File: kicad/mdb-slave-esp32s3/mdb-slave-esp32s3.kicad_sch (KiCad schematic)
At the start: 36 parts, among them J1 Conn_02x09_Odd_Even, J2 MDB_Connector, P1 USB_C_Plug_USB2.0, SW1 Reset, SW2 Boot, U1 ESP32-S3, U2 LM317_SOT-223, U4 PC817, U5 PC817, Y1 Crystal

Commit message: Refacting
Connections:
- net mdb_slave_receive renamed io4
- net mdb_slave_transmit renamed io5
- net vdd_spi: no longer names the net of U1.29 (VDD_SPI)
- no-connect marks 23 -> 24
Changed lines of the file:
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@@
+	)
+	(no_connect
+		(at 124.46 134.62)
 	)
 	(no_connect
@@
 	(wire
 		(pts
-			(xy 124.46 128.27) (xy 124.46 134.62)
-		)
-		(stroke
-			(width 0)
-			(type default)
-		)
-	)
-	(wire
-		(pts
 			(xy 165.1 170.18) (xy 167.64 170.18)
 		)
@@
 	(wire
 		(pts
-			(xy 165.1 167.64) (xy 186.69 167.64)
-		)
-		(stroke
-			(width 0)
-			(type default)
-		)
-	)
-	(wire
-		(pts
 			(xy 99.06 160.02) (xy 93.98 160.02)
 		)
@@
 	(wire
 		(pts
-			(xy 165.1 165.1) (xy 186.69 165.1)
-		)
-		(stroke
-			(width 0)
-			(type default)
-		)
-	)
-	(wire
-		(pts
 			(xy 165.1 195.58) (xy 167.64 195.58)
 		)
@@
 	(wire
 		(pts
+			(xy 165.1 165.1) (xy 167.64 165.1)
+		)
+		(stroke
+			(width 0)
+			(type default)
+		)
+	)
+	(wire
+		(pts
 			(xy 45.72 240.03) (xy 57.15 240.03)
 		)
@@
 		(pts
 			(xy 53.34 255.27) (xy 57.15 255.27)
+		)
+		(stroke
+			(width 0)
+			(type default)
+		)
+	)
+	(wire
+		(pts
+			(xy 165.1 167.64) (xy 167.64 167.64)
 		)
 		(stroke
@@
 		)
 	)
+	(label "io5"
+		(at 167.64 167.64 0)
+		(fields_autoplaced yes)
+		(effects
+			(font
+				(size 1.27 1.27)
+			)
+			(justify left bottom)
+		)
+	)
 	(label "io2"
 		(at 53.34 250.19 180)
@@
 		)
 	)
+	(label "io5"
+		(at 356.87 110.49 0)
+		(fields_autoplaced yes)
+		(effects
+			(font
+				(size 1.27 1.27)
+			)
+			(justify left bottom)
+		)
+	)
 	(label "io14"
 		(at 167.64 190.5 0)
@@
 		)
 	)
-	(label "mdb_slave_receive"
-		(at 186.69 165.1 0)
-		(fields_autoplaced yes)
-		(effects
-			(font
-				(size 1.27 1.27)
-			)
-			(justify left bottom)
-		)
-	)
 	(label "io10"
 		(at 73.66 245.11 0)
@@
 		)
 	)
+	(label "io4"
+		(at 167.64 165.1 0)
+		(fields_autoplaced yes)
+		(effects
+			(font
+				(size 1.27 1.27)
+			)
+			(justify left bottom)
+		)
+	)
 	(label "io6"
 		(at 167.64 170.18 0)
@@
 		)
 	)
-	(label "mdb_slave_receive"
-		(at 356.87 95.25 0)
-		(fields_autoplaced yes)
-		(effects
-			(font
-				(size 1.27 1.27)
-			)
-			(justify left bottom)
-		)
-	)
 	(label "io7"
 		(at 167.64 172.72 0)
@@
 		)
 	)
+	(label "io4"
+		(at 356.87 95.25 0)
+		(fields_autoplaced yes)
+		(effects
+			(font
+				(size 1.27 1.27)
+			)
+			(justify left bottom)
+		)
+	)
 	(label "io21"
 		(at 177.8 59.69 0)
@@
 		)
 	)
-	(label "vdd_spi"
-		(at 124.46 128.27 90)
-		(fields_autoplaced yes)
-		(effects
-			(font
-				(size 1.27 1.27)
-			)
-			(justify left bottom)
-		)
-	)
 	(label "mdb_master_receive"
 		(at 325.12 115.57 180)
@@
 		)
 	)
-	(label "mdb_slave_transmit"
-		(at 356.87 110.49 0)
-		(fields_autoplaced yes)
-		(effects
-			(font
-				(size 1.27 1.27)
-			)
-			(justify left bottom)
-		)
-	)
 	(label "io9"
 		(at 167.64 177.8 0)
@@
 		(fields_autoplaced yes)
 		(effects
-			(font
-				(size 1.27 1.27)
-			)
-			(justify left bottom)
-		)
-	)
-	(label "mdb_slave_transmit"
-		(at 186.69 167.64 0)
-		(fields_autoplaced yes)
-		(effects

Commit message: refacting
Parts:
- removed AE1: Antenna, RF_Antenna:Texas_SWRA117D_2.4GHz_Right, symbol Device:Antenna
- removed C1, C2, C3, C4, C5, C6: C, Capacitor_SMD:C_0603_1608Metric, symbol Device:C
- removed D1, D2: LED, LED_SMD:LED_0603_1608Metric, symbol Device:LED
- removed D4: D, Diode_SMD:D_SOD-123, symbol Device:D
- removed L1: 47nH, Inductor_SMD:L_0603_1608Metric, symbol Device:L
- removed P1: USB_C_Plug_USB2.0, Connector_USB:USB_C_Receptacle_G-Switch_GT-USB-7010ASV, symbol Connector:USB_C_Plug_USB2.0
- removed R1, R10, R2, R3, R4, R5, R6, R7, R9: R, Resistor_SMD:R_0603_1608Metric, symbol Device:R
- removed SW2: Boot, Button_Switch_SMD:SW_Tactile_SPST_NO_Straight_CK_PTS636Sx25SMTRLFS, symbol Switch:SW_Push
- removed U1: ESP32-S3, Package_DFN_QFN:QFN-56-1EP_7x7mm_P0.4mm_EP5.6x5.6mm, symbol PCM_Espressif:ESP32-S3
- removed Y1: Crystal, Crystal:Crystal_HC49-4H_Vertical, symbol Device:Crystal
- added AE2: Antenna, RF_Antenna:Texas_SWRA117D_2.4GHz_Right, symbol Device:Antenna
- added C10, C11, C12, C13, C14, C15, C8: C, Capacitor_SMD:C_0603_1608Metric, symbol Device:C
- added D3: D, Diode_SMD:D_SOD-123, symbol Device:D
- added D6, D7: LED, LED_SMD:LED_0603_1608Metric, symbol Device:LED
- added L2: 47nH, Inductor_SMD:L_0603_1608Metric, symbol Device:L
- added P2: USB_C_Plug_USB2.0, Connector_USB:USB_C_Receptacle_G-Switch_GT-USB-7010ASV, symbol Connector:USB_C_Plug_USB2.0
- added R15, R16, R17, R18, R19, R20, R22, R23, R24: R, Resistor_SMD:R_0603_1608Metric, symbol Device:R
- added SW3: SW_Push, Button_Switch_SMD:SW_Tactile_SPST_NO_Straight_CK_PTS636Sx25SMTRLFS, symbol Switch:SW_Push
- added TP1, TP2, TP3: TestPoint, TestPoint:TestPoint_Pad_D1.0mm, symbol Connector:TestPoint
- added U3: ESP32-S3, Package_DFN_QFN:QFN-56-1EP_7x7mm_P0.4mm_EP5.6x5.6mm, symbol PCM_Espressif:ESP32-S3
- added U6: W25Q32JVSS, Package_SON:WSON-8-1EP_8x6mm_P1.27mm_EP3.4x4.3mm, symbol Memory_Flash:W25Q32JVSS
- added Y2: Crystal, Crystal:Crystal_HC49-4H_Vertical, symbol Device:Crystal
- SW1: value Reset -> SW_Push
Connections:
- net +3V3: now also J1.16 (Pin_16), C12.2, C13.2, C14.2, D7.2 (A), R15.1, R17.2, TP1.1, U3.2 (VDD3P3), U3.20 (VDD3P3_RTC), U3.3 (VDD3P3), U3.46 (VDD3P3_CPU), U3.55 (VDDA), U3.56 (VDDA)
- net GND: now also SW1.2, C10.1, C11.1, C12.1, C13.1, C14.1, C15.2, L2.2, P2.A1 (GND), P2.A12 (GND), P2.B1 (GND), P2.B12 (GND), R16.2, R18.2, R19.2, R20.2, R22.1, R23.1, R24.2, SW3.1, TP3.1, U3.57 (GND), U6.4 (GND); no longer J1.16 (Pin_16), SW1.1
- net boot: now also SW1.1, R17.1, U3.5 (GPIO0/BOOT)
- net io1: now also U3.6 (GPIO1/ADC1_CH0)
- net io10: now also U3.15 (GPIO10/ADC1_CH9)
- net io11: now also U3.16 (GPIO11/ADC2_CH0)
- net io12: now also U3.17 (GPIO12/ADC2_CH1)
- net io13: now also U3.18 (GPIO13/ADC2_CH2)
- net io14: now also U3.19 (GPIO14/ADC2_CH3)
- net io17: now also U3.23 (GPIO17/ADC2_CH6)
- net io18: now also U3.24 (GPIO18/ADC2_CH7)
- net io2: now also U3.7 (GPIO2/ADC1_CH1)
- net io21: now also D6.2 (A), U3.27 (GPIO21)
- net io4: now also U3.9 (GPIO4/ADC1_CH3)
- net io5: now also U3.10 (GPIO5/ADC1_CH4)
- net io6: now also U3.11 (GPIO6/ADC1_CH5)
- net io7: now also U3.12 (GPIO7/ADC1_CH6)
- net io8: now also U3.13 (GPIO8/ADC1_CH7)
- net io9: now also U3.14 (GPIO9/ADC1_CH8)
- net u0rxd: now also U3.50 (U0RXD/PROG/GPIO44)
- net u0txd: now also U3.49 (U0TXD/PROG/GPIO43)
- net usb+: now also P2.A6 (D+), U3.26 (GPIO20/USB_D+/ADC2_CH9)
- net usb-: now also P2.A7 (D-), U3.25 (GPIO19/USB_D-/ADC2_CH8)
- net +36V renamed vin
- net vin: now also D3.1 (K), TP2.1
- new net: R16.1, U3.52 (GPIO46)
- new net: D7.1 (K), R23.2
- new net: D3.2 (A), P2.A4 (VBUS), P2.A9 (VBUS), P2.B4 (VBUS), P2.B9 (VBUS)
- new net: C10.2, U3.53 (XTAL_N), Y2.2
- new net: C8.2, U3.1 (LNA_IN/RF)
- new net: R15.2, SW3.2, U3.4 (CHIP_PU/RESET)
- new net: R18.1, U3.51 (GPIO45)
- new net: C11.2, U3.54 (XTAL_P), Y2.1
- new net: P2.A5 (CC), R24.1
- new net: P2.B5 (VCONN), R20.1
- new net: P2.S1 (SHIELD), R19.1
- new net: D6.1 (K), R22.2
- new net: AE2.1 (A), C8.1, L2.1
- new net spiclk: U3.33 (SPICLK/GPIO30), U6.6 (CLK)
- new net spics0: U3.32 (SPICS0/GPIO29), U6.1 (~{CS})
- new net spid: U3.35 (SPID/GPIO32), U6.5 (DI(IO0))
- new net spihd: U3.30 (SPIHD/GPIO27), U6.7 (IO3)
- new net spiq: U3.34 (SPIQ/GPIO31), U6.2 (DO(IO1))
- new net spiwp: U3.31 (SPIWP/GPIO28), U6.3 (IO2)
- new net vdd_spi: C15.1, U3.29 (VDD_SPI), U6.8 (VCC)
- no-connect marks 24 -> 17
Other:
- note added: "ESP32-S3R8"
- note added: "W25Q256JVEIQ"
- note removed: "ESP32-S3FH4R2"
- moved on the sheet: C7, R14, R8, U2

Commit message: Refacting
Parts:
- removed C15: C, Capacitor_SMD:C_0603_1608Metric, symbol Device:C
- removed J1: Conn_02x09_Odd_Even, Connector_PinHeader_2.54mm:PinHeader_2x09_P2.54mm_Vertical, symbol Connector_Generic:Conn_02x09_Odd_Even
- removed U6: W25Q32JVSS, Package_SON:WSON-8-1EP_8x6mm_P1.27mm_EP3.4x4.3mm, symbol Memory_Flash:W25Q32JVSS
- added J3: Conn_02x11_Odd_Even, Connector_PinHeader_2.54mm:PinHeader_2x11_P2.54mm_Vertical, symbol Connector_Generic:Conn_02x11_Odd_Even
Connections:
- net +3V3: now also J3.16 (Pin_16)
- net GND: now also J3.1 (Pin_1), J3.18 (Pin_18), J3.20 (Pin_20)
- net io1: now also J3.7 (Pin_7)
- net io10: now also J3.6 (Pin_6)
- net io11: now also J3.8 (Pin_8)
- net io12: now also J3.10 (Pin_10)
- net io13: now also J3.12 (Pin_12)
- net io14: now also J3.14 (Pin_14)
- net io17: now also J3.19 (Pin_19)
- net io18: now also J3.21 (Pin_21)
- net io2: now also J3.9 (Pin_9)
- net io4: now also J3.11 (Pin_11)
- net io5: now also J3.13 (Pin_13)
- net io6: now also J3.15 (Pin_15)
- net io7: now also J3.17 (Pin_17)
- net io8: now also J3.2 (Pin_2)
- net io9: now also J3.4 (Pin_4)
- net u0rxd: now also J3.5 (Pin_5)
- net u0txd: now also J3.3 (Pin_3)
- net vin: now also J3.22 (Pin_22)
- net spiclk: no longer names the net of U3.33 (SPICLK/GPIO30)
- net spics0: no longer names the net of U3.32 (SPICS0/GPIO29)
- net spid: no longer names the net of U3.35 (SPID/GPIO32)
- net spihd: no longer names the net of U3.30 (SPIHD/GPIO27)
- net spiq: no longer names the net of U3.34 (SPIQ/GPIO31)
- net spiwp: no longer names the net of U3.31 (SPIWP/GPIO28)
- net vdd_spi: no longer names the net of U3.29 (VDD_SPI)
- no-connect marks 17 -> 24
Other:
- note removed: "W25Q256JVEIQ"

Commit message: Refacting
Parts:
- U3: value ESP32-S3 -> ESP32-S3FH4R2
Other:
- note removed: "ESP32-S3R8"
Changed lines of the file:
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@@
-		)
-	)
-	(text "ESP32-S3R8"
-		(exclude_from_sim no)
-		(at 137.16 110.49 0)
-		(effects
-			(font
-				(size 1.27 1.27)
-			)
-			(justify left bottom)
 		)
 	)
@@
 			)
 		)
-		(property "Value" "ESP32-S3"
+		(property "Value" "ESP32-S3FH4R2"
 			(at 121.5741 194.31 0)
 			(effects

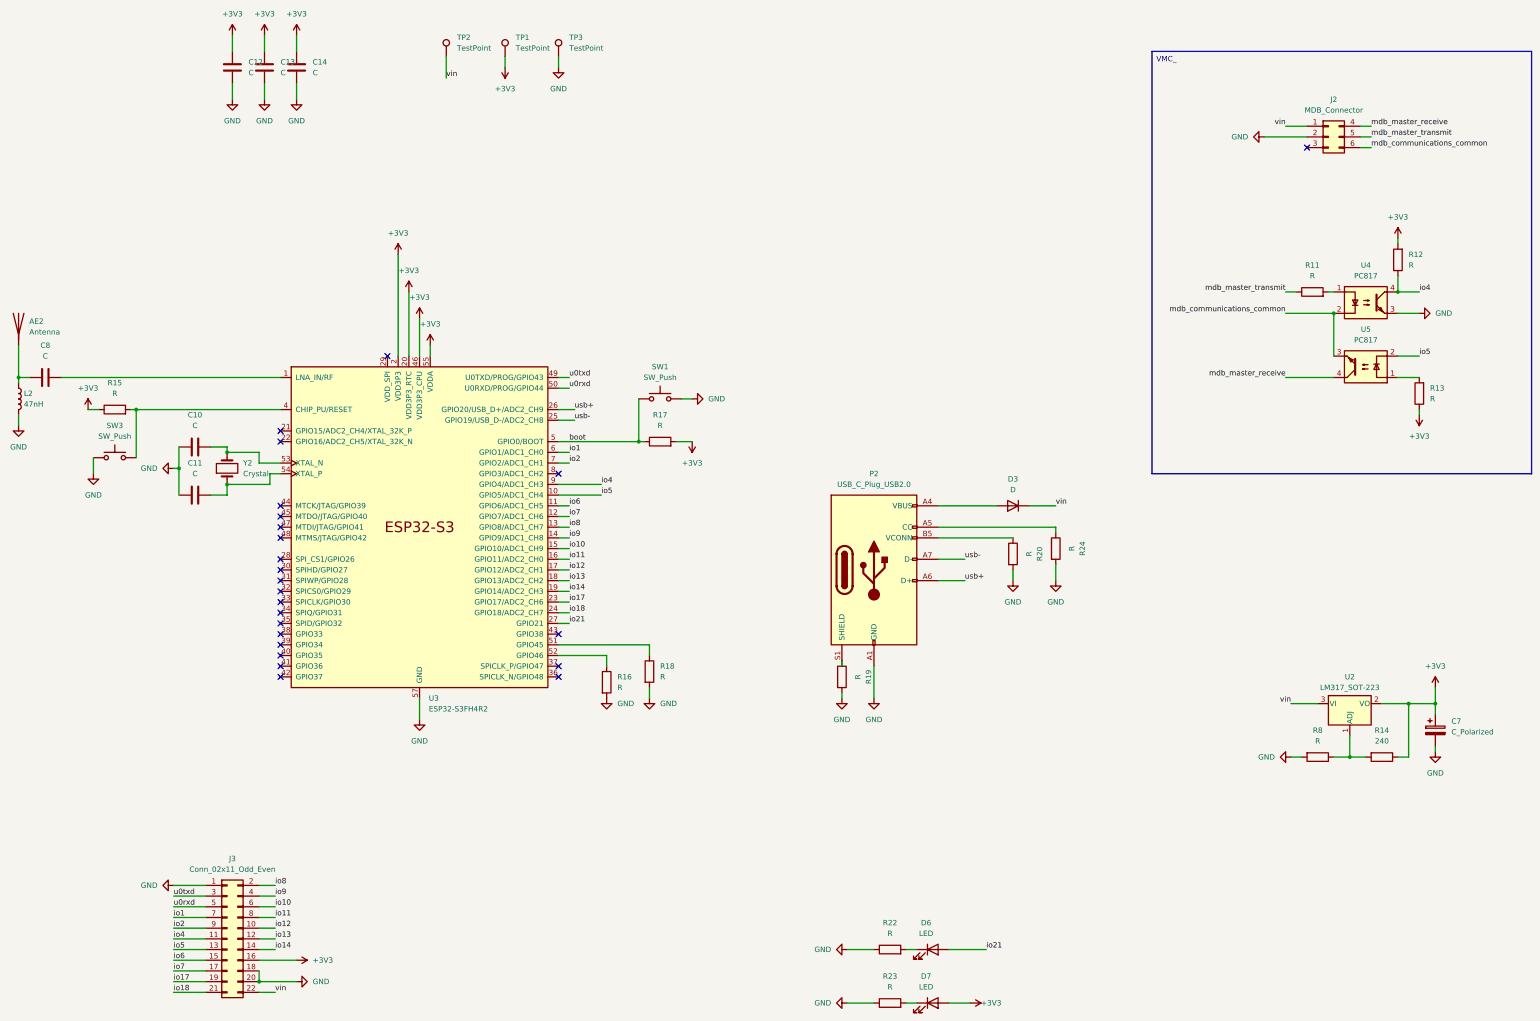
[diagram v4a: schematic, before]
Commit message: Updating POM list
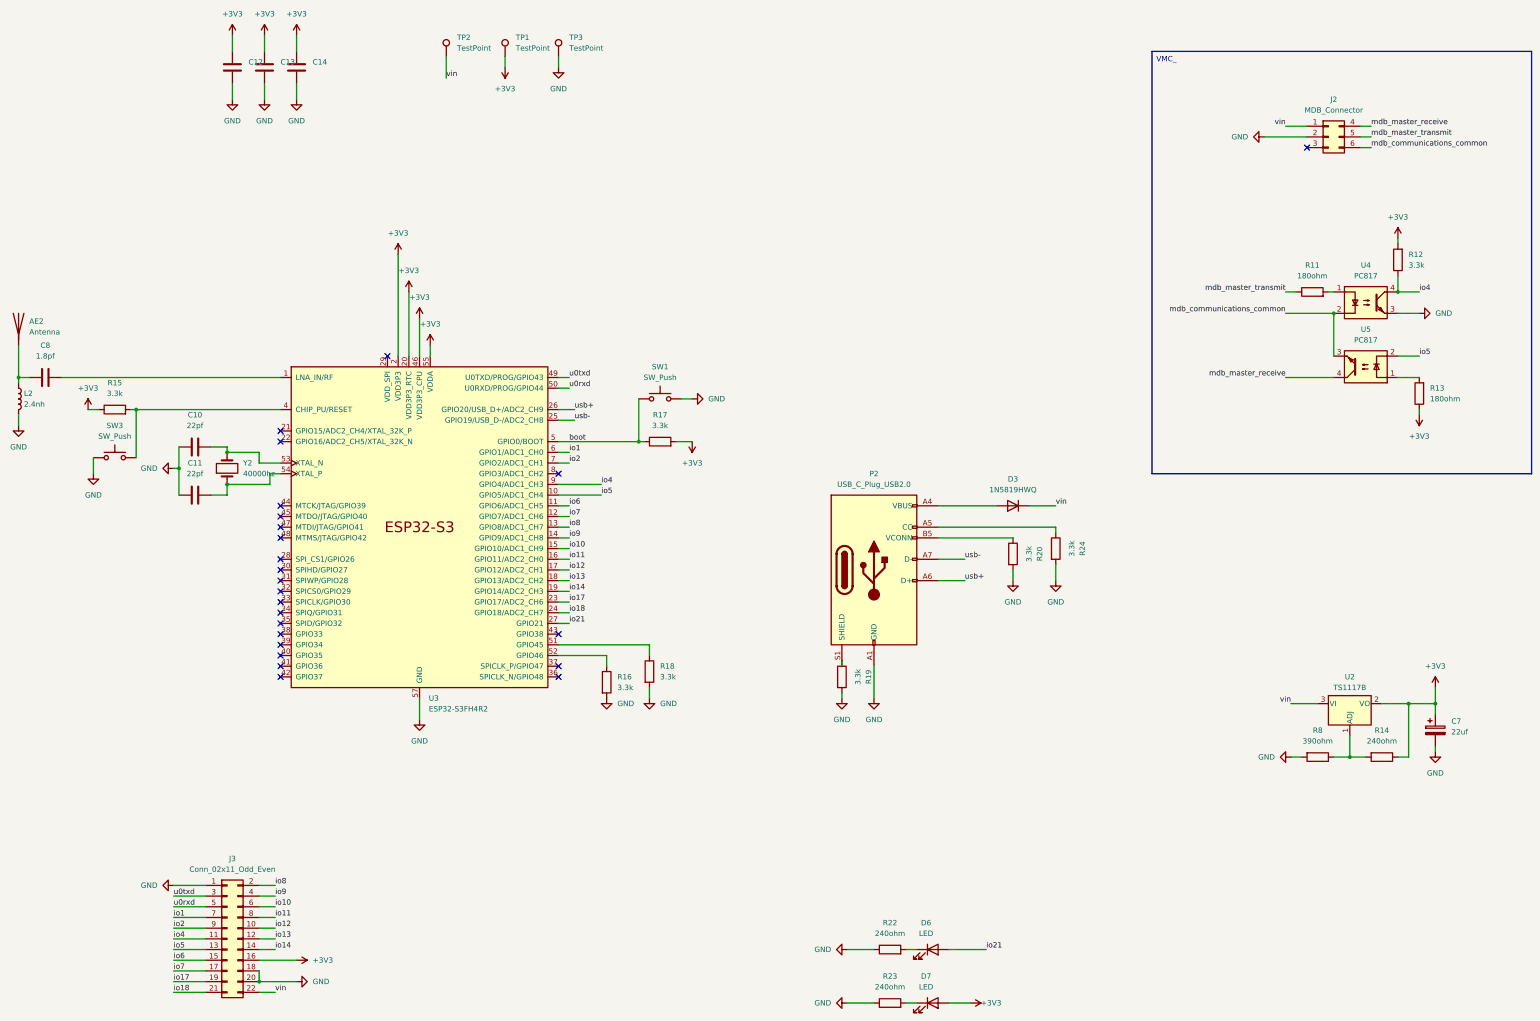
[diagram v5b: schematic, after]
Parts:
- C10, C11: value C -> 22pf
- C7: value C_Polarized -> 22uf
- C8: value C -> 1.8pf
- D3: value D -> 1N5819HWQ
- L2: value 47nH -> 2.4nh
- R11, R13: value R -> 180ohm
- R12, R15, R16, R17, R18, R19, R20, R24: value R -> 3.3k
- R14: value 240 -> 240ohm
- R22, R23: value R -> 240ohm
- R8: value R -> 390ohm
- U2: value LM317_SOT-223 -> TS1117B
- Y2: value Crystal -> 40000hz
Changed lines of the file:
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@@
 			)
 		)
-		(property "Value" "R"
+		(property "Value" "3.3k"
 			(at 166.37 189.23 0)
 			(effects
@@
 			)
 		)
-		(property "Value" "R"
+		(property "Value" "3.3k"
 			(at 354.33 88.8999 0)
 			(effects
@@
 			)
 		)
-		(property "Value" "D"
+		(property "Value" "1N5819HWQ"
 			(at 260.35 142.24 0)
 			(effects
@@
 				)
 				(justify right)
+				(hide yes)
 			)
 		)
@@
 			)
 		)
-		(property "Value" "C"
+		(property "Value" "22pf"
 			(at 66.04 127 90)
 			(effects
@@
 			)
 		)
-		(property "Value" "R"
+		(property "Value" "3.3k"
 			(at 46.99 119.38 90)
 			(effects
@@
 			)
 		)
-		(property "Value" "C_Polarized"
+		(property "Value" "22uf"
 			(at 364.49 199.7709 0)
 			(effects
@@
 			)
 		)
-		(property "Value" "R"
+		(property "Value" "3.3k"
 			(at 176.53 186.69 0)
 			(effects
@@
 			)
 		)
-		(property "Value" "C"
+		(property "Value" "1.8pf"
 			(at 30.48 110.49 90)
 			(effects
@@
 			)
 		)
-		(property "Value" "R"
+		(property "Value" "3.3k"
 			(at 176.53 127 90)
 			(effects
@@
 			)
 		)
-		(property "Value" "240"
+		(property "Value" "240ohm"
 			(at 347.98 201.93 90)
 			(effects
@@
 			)
 		)
-		(property "Value" "R"
+		(property "Value" "240ohm"
 			(at 231.14 260.35 90)
 			(effects
@@
 			)
 		)
-		(property "Value" "C"
+		(property "Value" "22pf"
 			(at 66.04 138.43 90)
 			(effects
@@
 			)
 		)
-		(property "Value" "47nH"
+		(property "Value" "2.4nh"
 			(at 25.4 121.92 0)
 			(effects
@@
 			)
 		)
-		(property "Value" "R"
+		(property "Value" "3.3k"
 			(at 223.52 186.69 90)
 			(effects
@@
 				)
 				(justify right)
+				(hide yes)
 			)
 		)
@@
 			)
 		)
-		(property "Value" "R"
+		(property "Value" "390ohm"
 			(at 332.74 201.93 90)
 			(effects
@@
 			)
 		)
-		(property "Value" "LM317_SOT-223"
+		(property "Value" "TS1117B"
 			(at 340.36 189.23 0)
 			(effects
@@
 			)
 		)
-		(property "Value" "R"
+		(property "Value" "180ohm"
 			(at 331.47 91.44 90)
 			(effects
@@
 			)
 		)
-		(property "Value" "Crystal"
+		(property "Value" "40000hz"
 			(at 77.47 138.43 90)
 			(effects
@@
 			)
 		)
-		(property "Value" "R"
+		(property "Value" "3.3k"
 			(at 274.32 156.21 90)
 			(effects
@@
 			)
 		)
-		(property "Value" "R"
+		(property "Value" "3.3k"
 			(at 264.16 157.48 90)
 			(effects
@@
 				)
 				(justify right)
+				(hide yes)
 			)
 		)
@@
 			)
 		)
-		(property "Value" "R"
+		(property "Value" "180ohm"
 			(at 359.41 120.6499 0)
 			(effects
@@
 			)
 		)
-		(property "Value" "R"
+		(property "Value" "240ohm"
 			(at 231.14 247.65 90)
 			(effects
